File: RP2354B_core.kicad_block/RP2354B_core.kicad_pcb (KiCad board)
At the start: 2 copper layers, 22 parts, among them U1 RP2350_80QFN, Y1 ABM8-272-T3

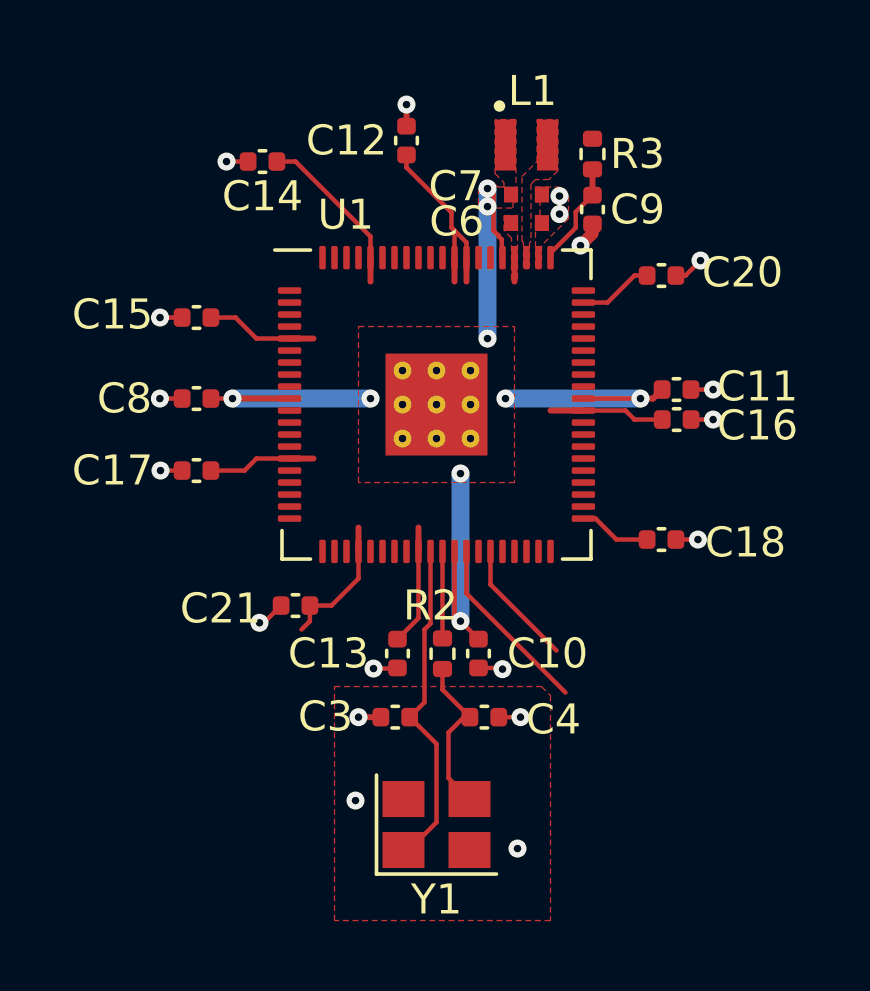
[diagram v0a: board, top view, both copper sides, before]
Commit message: Renumber block components sequentially (C1..C17, R1..R2)
Closes refdes gaps that caused duplicate footprints when importing the
block PCB into parent projects via re-link by refdes.
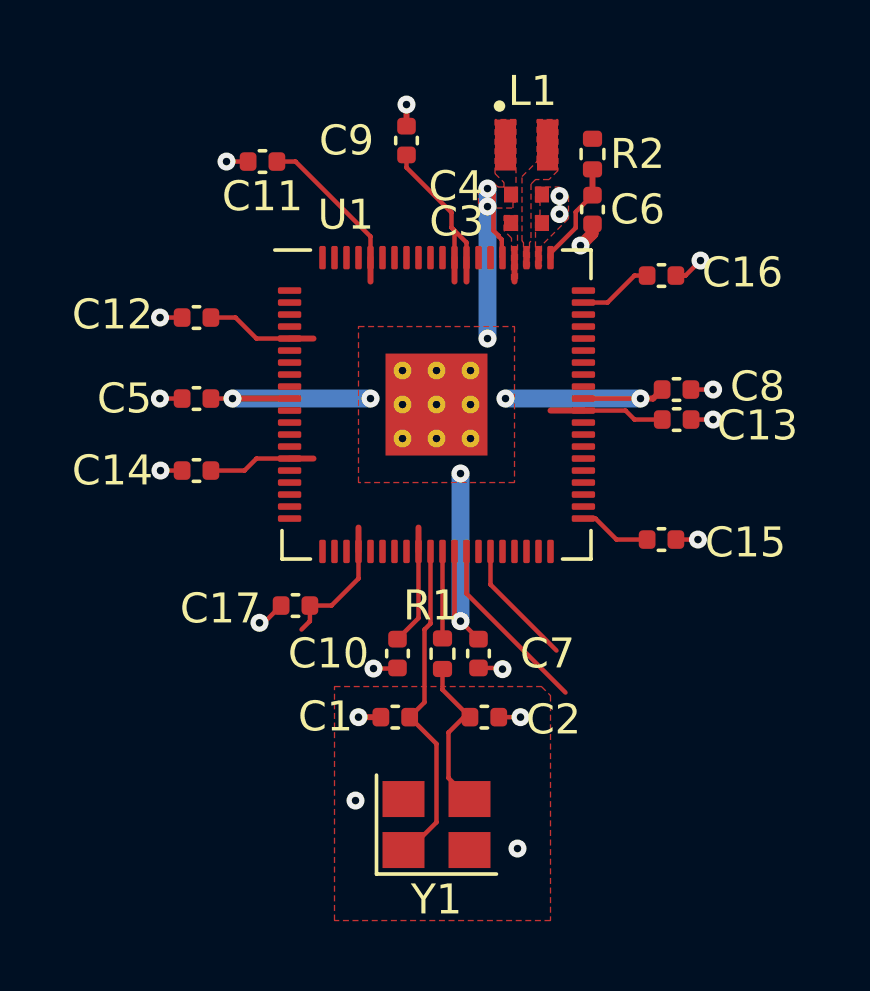
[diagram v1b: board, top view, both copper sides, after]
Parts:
- renumbered C3 to C1, C13 to C10, C14 to C11, C15 to C12, C16 to C13, C17 to C14, C18 to C15, C20 to C16, C21 to C17, C4 to C2, C6 to C3, C7 to C4, C8 to C5, C9 to C6, C10 to C7, C11 to C8, C12 to C9, R2 to R1, R3 to R2
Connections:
- net /GPIO40_ADC0 renamed /GPIO40
- net /GPIO41_ADC1 renamed /GPIO41
- net /GPIO42_ADC2 renamed /GPIO42
- net /GPIO43_ADC3 renamed /GPIO43
- net /GPIO44_ADC4 renamed /GPIO44
- net /GPIO45_ADC5 renamed /GPIO45
- net /GPIO46_ADC6 renamed /GPIO46
- net /GPIO47_ADC7 renamed /GPIO47
- net /SWD renamed /SWDIO
- U1 pad 66: unconnected-(U1-USB_DM-Pad66) -> /USB_DM
- U1 pad 67: unconnected-(U1-USB_DP-Pad67) -> /USB_DP
